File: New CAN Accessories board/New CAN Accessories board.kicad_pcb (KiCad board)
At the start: 2 copper layers, 110 x 86 mm, 108 parts, among them J1 39301040, J10 39301040, J11 ATF13-2P-BM03, J12 Conn_01x02_Pin, J13 Conn_01x12_Pin, J14 Conn_01x08_Pin, J2 39301040, J3 39301040, J4 39301040, J5 39301040, J6 39301040, J7 39301040, J8 39301040, J9 39301060, Q1 IRLML6344TRPBF, Q2 IRLML6344TRPBF, Q3 IRLML6344TRPBF, Q4 IRLML6344TRPBF, Q5 IRLML6344TRPBF, Q6 IRLML6344TRPBF, Q7 IRLML6344TRPBF, Q8 IRLML6344TRPBF, T1 MCP2562FD-E_SN, U1 NUCLEO_L432KC

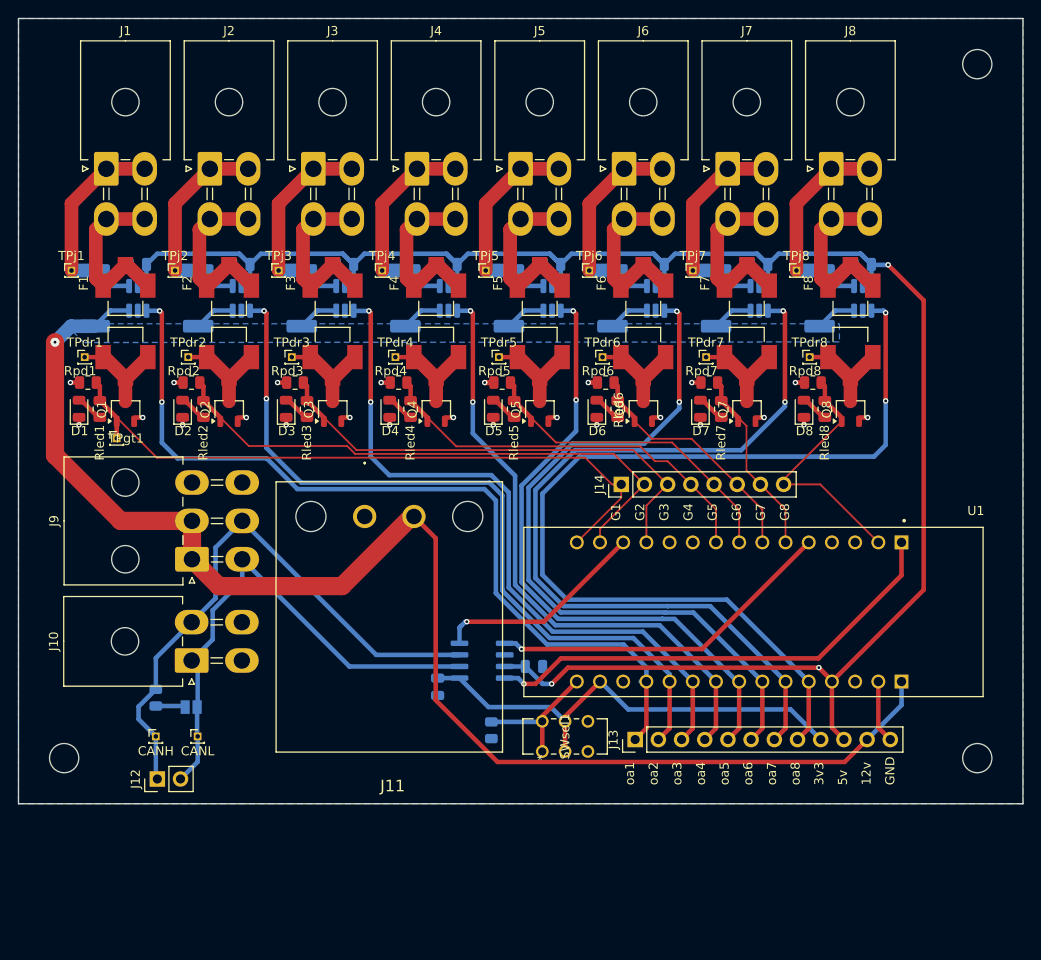
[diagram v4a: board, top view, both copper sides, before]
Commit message: added bulk cap
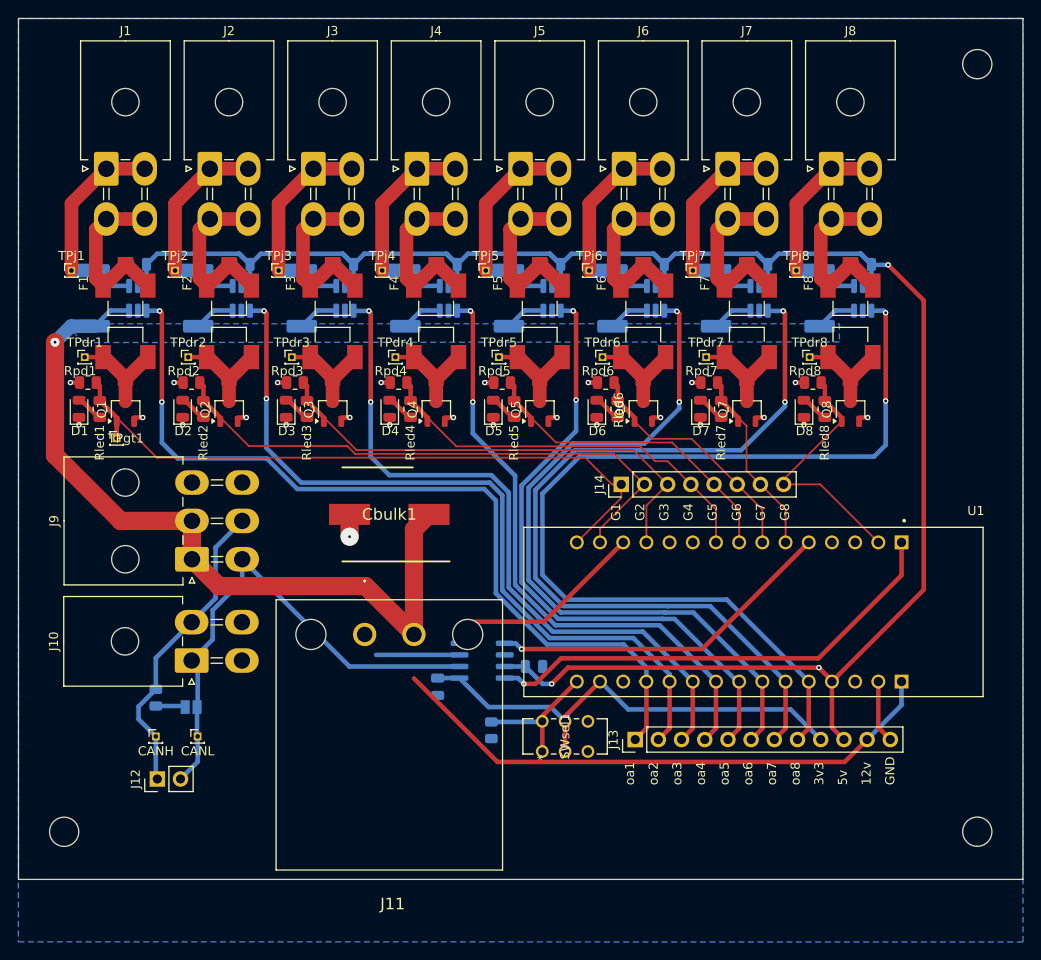
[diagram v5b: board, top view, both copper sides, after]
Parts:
- added Cbulk1: C_Polarized, footprint:CAPAE1030X1050M, F.Cu at (54.6, 68.3)
- moved J11 12.9 mm to (51.9, 81.5)
- moved H3 8.06 mm to (19.0, 103.1)
- moved H2 8.06 mm to (119.0, 103.1)
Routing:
- net /CANH: track 63.7 -> 42.9 mm
- net 12V: track 184.3 -> 179.6 mm
- net GND: track 52.9 -> 55.3 mm, vias 24 -> 25
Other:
- board size 110 x 86 mm -> 110 x 94.3 mm

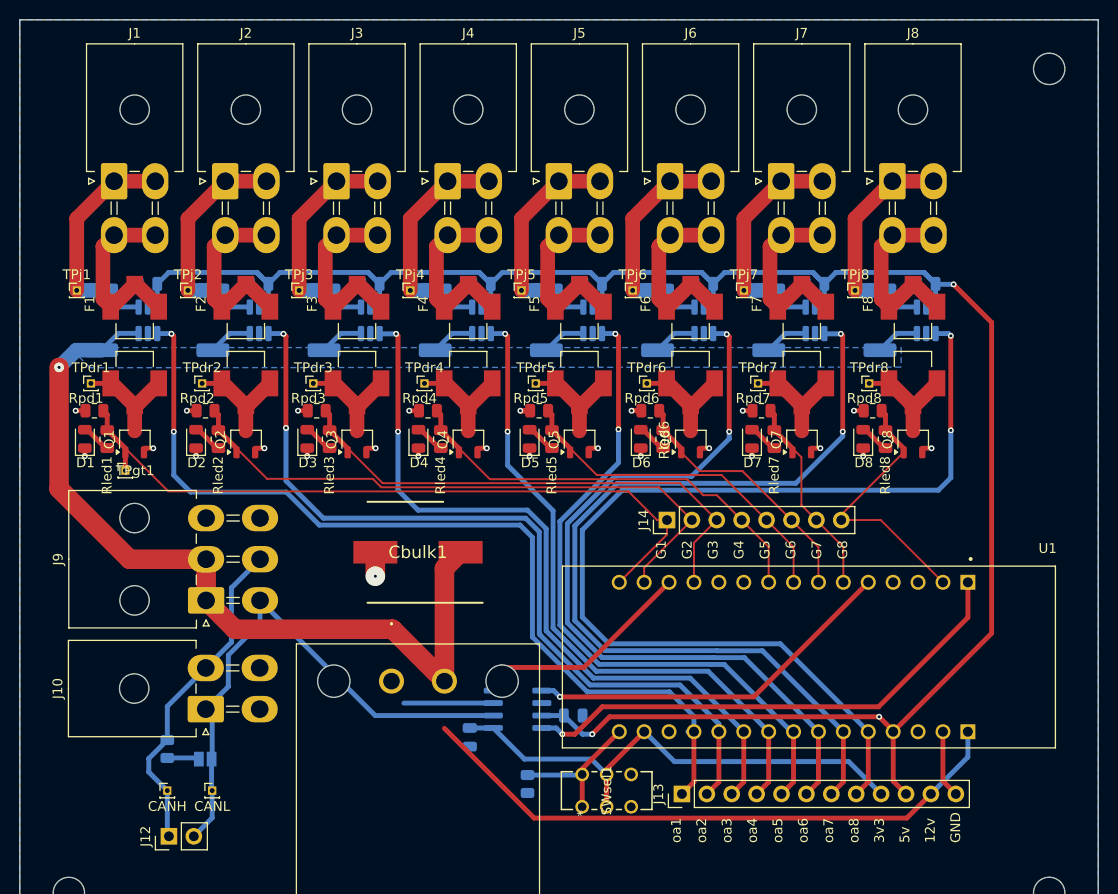
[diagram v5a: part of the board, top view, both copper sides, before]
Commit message: Added two 1x4 pin headers for J1-J8 - also fixed CAN module
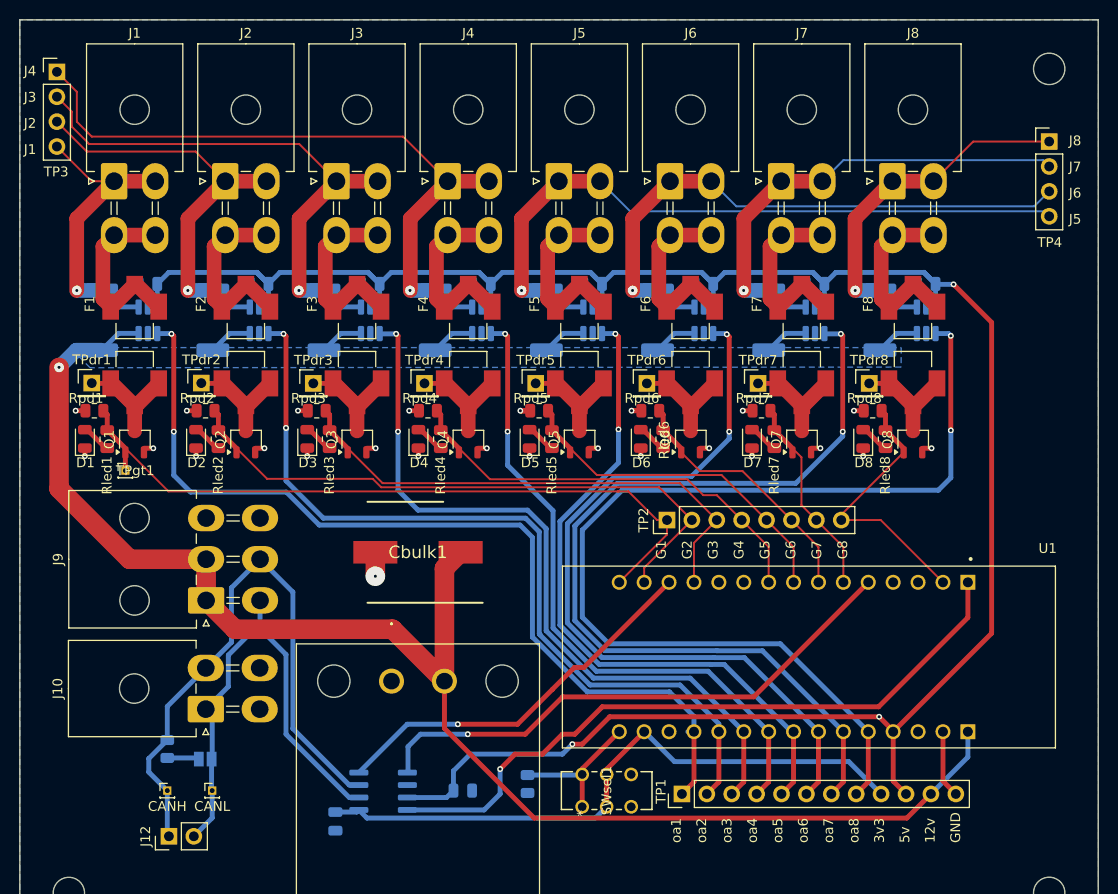
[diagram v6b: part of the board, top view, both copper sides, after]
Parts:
- removed TPj1, TPj2, TPj3, TPj4, TPj5, TPj6, TPj7, TPj8: TestPoint, Connector_PinHeader_1.00mm:PinHeader_1x01_P1.00mm_Vertical
- added TP3: Conn_01x04_Pin, Connector_PinHeader_2.54mm:PinHeader_1x04_P2.54mm_Vertical, F.Cu at (17.8, 19.3)
- added TP4: Conn_01x04_Pin, Connector_PinHeader_2.54mm:PinHeader_1x04_P2.54mm_Vertical, F.Cu at (119.0, 26.4)
- Cbulk1: value C_Polarized -> 270uF
- TPdr1, TPdr2, TPdr3, TPdr4, TPdr5, TPdr6, TPdr7, TPdr8: footprint Connector_PinHeader_1.00mm:PinHeader_1x01_P1.00mm_Vertical -> Connector_PinHeader_2.54mm:PinHeader_1x01_P2.54mm_Vertical
- moved Ctr2 16.2 mm to (46.2, 95.8)
- moved T1 16.1 mm to (51.1, 92.7)
- moved Ctr1 13.6 mm to (59.2, 92.6)
- moved TPdr1 0.09 mm to (21.3, 51.1)
- moved TPdr2 0.08 mm to (32.5, 51.1)
- renumbered J13 to TP1, J14 to TP2
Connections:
- net Net-(J1-Pin_1) renamed /TPj1
- net Net-(J2-Pin_1) renamed /TPj2
- net Net-(J3-Pin_1) renamed /TPj3
- net Net-(J4-Pin_1) renamed /TPj4
- net Net-(J5-Pin_1) renamed /TPj5
- net Net-(J6-Pin_1) renamed /TPj6
- net Net-(J7-Pin_1) renamed /TPj7
- net Net-(J8-Pin_1) renamed /TPj8
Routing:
- net /TPj5: track 23.9 -> 71.2 mm, vias 0 -> 1
- net /TPj4: track 23.9 -> 70.2 mm, vias 0 -> 1
- net /TPj6: track 23.9 -> 60.1 mm, vias 0 -> 1
- net /TPj3: track 23.9 -> 56.9 mm, vias 0 -> 1
- net /TPj7: track 23.9 -> 48.2 mm, vias 0 -> 1
- net /TPj2: track 23.9 -> 43.6 mm, vias 0 -> 1
- net /CANH: track 42.9 -> 61.6 mm
- net /CANTX: track 38.4 -> 56.6 mm
- net /CANRX: track 52.2 -> 70.4 mm
- net 5V: track 215.0 -> 231.8 mm
- net /STBY: track 23.5 -> 39.7 mm
- net /TPj8: track 23.9 -> 37.4 mm, vias 0 -> 1
- net /3V3: track 52.0 -> 64.6 mm
- net /TPj1: track 23.9 -> 31.2 mm, vias 0 -> 1
- net /CANL: track 56.1 -> 50.0 mm
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
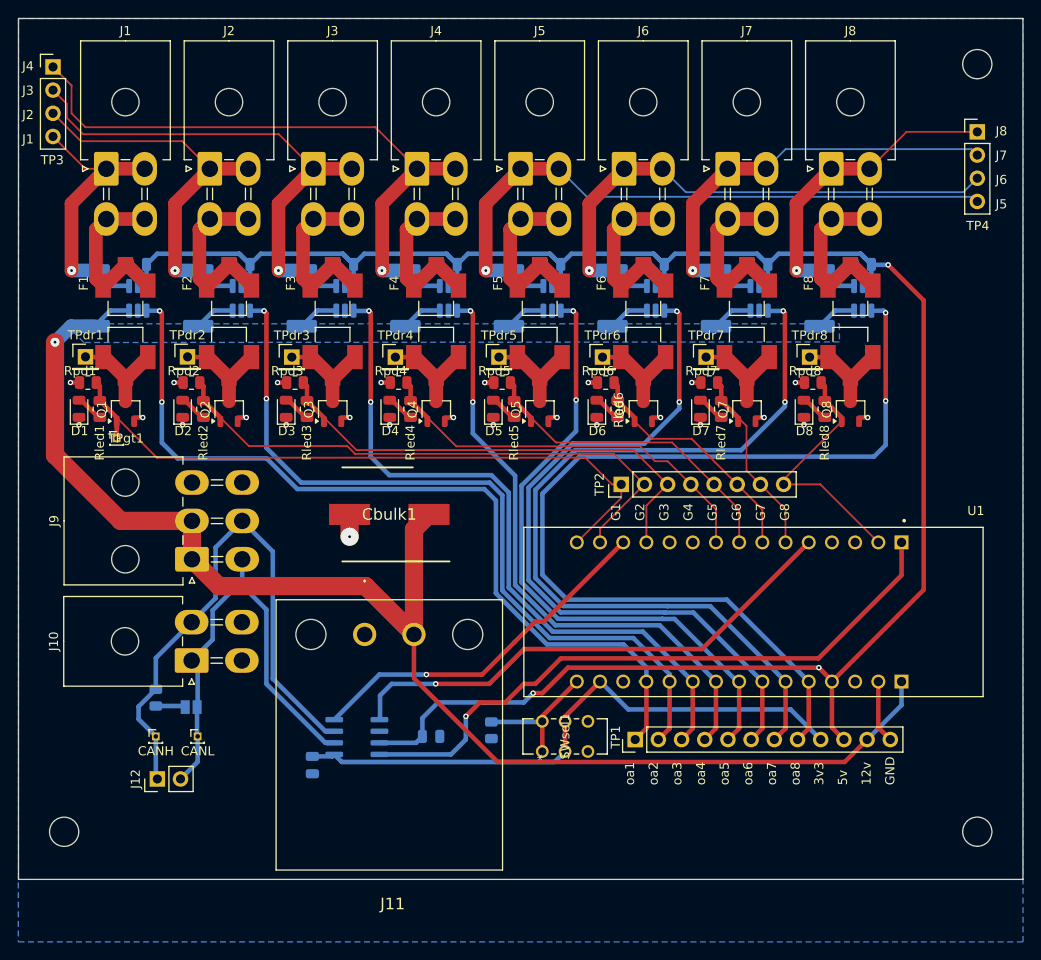
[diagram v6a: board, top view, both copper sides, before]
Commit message: few labelling changes
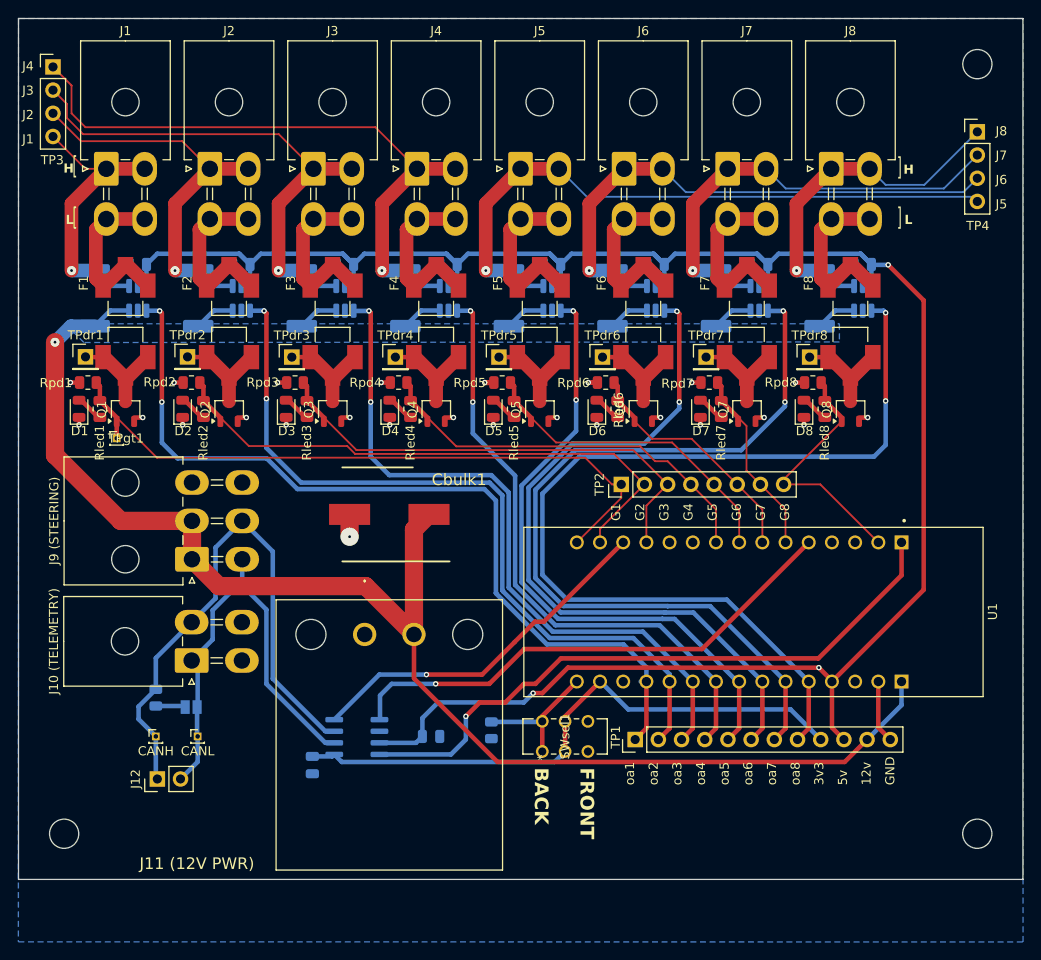
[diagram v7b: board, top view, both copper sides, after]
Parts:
- J10 (TELEMETRY): renamed from J10
- J11 (12V PWR): renamed from J11
- J9 (STEERING): renamed from J9
- moved H2 0.22 mm to (119.0, 103.3)
- moved H3 0.22 mm to (19.0, 103.3)
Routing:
- net /TPj8: track 37.4 -> 38.9 mm
- net /TPj7: track 48.2 -> 49.5 mm
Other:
- board text added: "BACK"
- board text added: "FRONT"
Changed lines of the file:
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@@
 		(tags "resistor")
 		(property "Reference" "Rpd1"
-			(at 0.852857 1.27 180)
+			(at 3.512857 -0.04 180)
 			(layer "F.SilkS")
 			(effects
@@
 		(tags "resistor")
 		(property "Reference" "Rpd4"
-			(at 0.852857 1.27 180)
+			(at 3.607143 0 180)
 			(layer "F.SilkS")
 			(effects
@@
 		(tags "resistor")
 		(property "Reference" "Rpd3"
-			(at 0.852857 1.27 180)
+			(at 3.545714 0.02 180)
 			(layer "F.SilkS")
 			(effects
@@
 			(layer "F.Fab")
 		)
+		(fp_text user "["
+			(at -3.7 0.83 0)
+			(unlocked yes)
+			(layer "F.SilkS")
+			(effects
+				(font
+					(size 2 1)
+					(thickness 0.1)
+				)
+				(justify left bottom)
+			)
+		)
+		(fp_text user "L"
+			(at -4.461905 6.164 0)
+			(unlocked yes)
+			(layer "F.SilkS")
+			(effects
+				(font
+					(size 1 1)
+					(thickness 0.2)
+					(bold yes)
+				)
+				(justify left bottom)
+			)
+		)
+		(fp_text user "["
+			(at -3.7 6.4545 0)
+			(unlocked yes)
+			(layer "F.SilkS")
+			(effects
+				(font
+					(size 2 1)
+					(thickness 0.1)
+				)
+				(justify left bottom)
+			)
+		)
+		(fp_text user "H"
+			(at -4.7 0.5395 0)
+			(unlocked yes)
+			(layer "F.SilkS")
+			(effects
+				(font
+					(size 1 1)
+					(thickness 0.2)
+					(bold yes)
+				)
+				(justify left bottom)
+			)
+		)
 		(fp_text user "${REFERENCE}"
 			(at 2.1 -13.2 0)
@@
 		(at 94.488 78.994 -90)
 		(property "Reference" "U1"
-			(at -11.08 -24.355 180)
+			(at -0.034 -26.202 90)
 			(layer "F.SilkS")
 			(effects
@@
 		(tags "resistor")
 		(property "Reference" "Rpd6"
-			(at 0.852857 1.27 180)
+			(at 3.53 -0.03 180)
 			(layer "F.SilkS")
 			(effects
@@
 	(footprint "MountingHole:MountingHole_3.2mm_M3_ISO14580"
 		(layer "F.Cu")
-		(at 19 103.065)
+		(at 19 103.28)
 		(descr "Mounting Hole 3.2mm, M3, no annular, generated by kicad-footprint-generator mountinghole.py")
 		(tags "mountinghole M3 ISO14580")
@@
 		(tags "resistor")
 		(property "Reference" "Rpd7"
-			(at 0.852857 1.27 180)
+			(at 3.481428 -0.1 180)
 			(layer "F.SilkS")
 			(effects
@@
 		(descr "Molex Mini-Fit Jr. Power Connectors, old mpn/engineering number: 5569-04A2, example for new mpn: 39-30-0040, 2 Pins per row, Mounting: Snap-in Plastic Peg PCB Lock (http://www.molex.com/pdm_docs/sd/039300020_sd.pdf), generated with kicad-footprint-generator")
 		(tags "connector Molex Mini-Fit_Jr horizontalplastic_peg")
-		(property "Reference" "J10"
+		(property "Reference" "J10 (TELEMETRY)"
 			(at 2.1 -15.1 90)
 			(layer "F.SilkS")
@@
 		(descr "ATF13-2P-BM03-1")
 		(tags "Connector")
-		(property "Reference" "J11"
-			(at 3.06 29.51 0)
+		(property "Reference" "J11 (12V PWR)"
+			(at -18.37 25.095 0)
 			(layer "F.SilkS")
 			(effects
@@
 		(descr "Molex Mini-Fit Jr. Power Connectors, old mpn/engineering number: 5569-06A2, example for new mpn: 39-30-0060, 3 Pins per row, Mounting: Snap-in Plastic Peg PCB Lock (http://www.molex.com/pdm_docs/sd/039300020_sd.pdf), generated with kicad-footprint-generator")
 		(tags "connector Molex Mini-Fit_Jr horizontalplastic_peg")
-		(property "Reference" "J9"
+		(property "Reference" "J9 (STEERING)"
 			(at 4.2 -15.1 90)
 			(layer "F.SilkS")
@@
 		(tags "resistor")
 		(property "Reference" "Rpd8"
-			(at 0.852857 1.27 180)
+			(at 3.502857 0.02 180)
 			(layer "F.SilkS")
 			(effects
@@
 		(tags "resistor")
 		(property "Reference" "Rpd5"
-			(at 0.852857 1.27 180)
+			(at 3.558571 -0.03 180)
 			(layer "F.SilkS")
 			(effects
@@
 			(layer "F.Fab")
 		)
+		(fp_text user "L"
+			(at 8.019047 6.164 0)
+			(unlocked yes)
+			(layer "F.SilkS")
+			(effects
+				(font
+					(size 1 1)
+					(thickness 0.2)
+					(bold yes)
+				)
+				(justify left bottom)
+			)
+		)
+		(fp_text user "H"
+			(at 7.9 0.664 0)
+			(unlocked yes)
+			(layer "F.SilkS")
+			(effects
+				(font
+					(size 1 1)
+					(thickness 0.2)
+					(bold yes)
+				)
+				(justify left bottom)
+			)
+		)
+		(fp_text user "]"
+			(at 7.2 6.4545 0)
+			(unlocked yes)
+			(layer "F.SilkS")
+			(effects
+				(font
+					(size 2 1)
+					(thickness 0.1)
+				)
+				(justify left bottom)
+			)
+		)
+		(fp_text user "]"
+			(at 7.2 0.9545 0)
+			(unlocked yes)
+			(layer "F.SilkS")
+			(effects
+				(font
+					(size 2 1)
+					(thickness 0.1)
+				)
+				(justify left bottom)
+			)
+		)
 		(fp_text user "${REFERENCE}"
 			(at 2.1 -13.2 0)
@@
 		(tags "Capacitor Polarised")
 		(property "Reference" "Cbulk1"
-			(at 0 0 180)
+			(at -7.65 3.8 180)
 			(layer "F.SilkS")
 			(effects
@@
 			(layer "F.Fab")
 		)
-		(fp_text user "${REFERENCE}"
-			(at 0 0 180)
-			(layer "F.Fab")
-			(effects
-				(font
-					(size 1.27 1.27)
-					(thickness 0.254)
-				)
-			)
-		)
 		(pad "1" smd rect
 			(at -4.35 0 270)
@@
 	(footprint "MountingHole:MountingHole_3.2mm_M3_ISO14580"
 		(layer "F.Cu")
-		(at 119 103.055)
+		(at 119 103.28)
 		(descr "Mounting Hole 3.2mm, M3, no annular, generated by kicad-footprint-generator mountinghole.py")
 		(tags "mountinghole M3 ISO14580")
@@
 	(footprint "MountingHole:MountingHole_3.2mm_M3_ISO14580"
 		(layer "F.Cu")
-		(at 119 19)
+		(at 119.01 19)
 		(descr "Mounting Hole 3.2mm, M3, no annular, generated by kicad-footprint-generator mountinghole.py")
 		(tags "mountinghole M3 ISO14580")
@@
 		(tags "resistor")
 		(property "Reference" "Rpd2"
-			(at 0.852857 1.27 180)
+			(at 3.484286 0.05 180)
 			(layer "F.SilkS")
 			(effects
@@
 		(layer "Edge.Cuts")
 	)
+	(gr_text "FRONT\n"
+		(at 75.364 96.03 270)
+		(layer "F.SilkS")
+		(effects
+			(font
+				(size 1.5 1.5)
+				(thickness 0.3)
+				(bold yes)
+			)
+			(justify left bottom)
+		)
+	)
+	(gr_text "BACK\n"
+		(at 70.364 96.03 270)
+		(layer "F.SilkS")
+		(effects
+			(font
+				(size 1.5 1.5)
+				(thickness 0.3)
+				(bold yes)
+			)
+			(justify left bottom)
+		)
+	)
 	(segment
 		(start 38.004286 57.7)
@@
 	)
 	(segment
-		(start 119 28.956)
-		(end 118.353 28.309)
-		(width 0.2)
-		(layer "B.Cu")
-		(net 65)
-	)
-	(segment
 		(start 92.071428 43.28)
 		(end 94.156477 43.28)
@@
 	)
 	(segment
-		(start 98.012428 28.309)
+		(start 115.337 32.619)
+		(end 98.020428 32.619)
+		(width 0.2)
+		(layer "B.Cu")
+		(net 65)
+	)
+	(segment
+		(start 98.020428 32.619)
 		(end 95.861428 30.46)
 		(width 0.2)
@@
 	)
 	(segment
-		(start 118.353 28.309)
-		(end 98.012428 28.309)
+		(start 119 28.956)
+		(end 115.337 32.619)
 		(width 0.2)
 		(layer "B.Cu")
@@
 	)
 	(segment
-		(start 119 26.416)
-		(end 111.246857 26.416)
-		(width 0.2)
-		(layer "F.Cu")
-		(net 66)
-	)
-	(segment
-		(start 111.246857 26.416)
-		(end 107.202857 30.46)
-		(width 0.2)
-		(layer "F.Cu")
-		(net 66)
-	)
-	(segment
 		(start 99.192857 41.61)
 		(end 99.192857 34.27)
@@
 	)
 	(segment
+		(start 108.960857 32.218)
+		(end 107.202857 30.46)
+		(width 0.2)
+		(layer "B.Cu")
+		(net 66)
+	)
+	(segment
+		(start 119 26.416)
+		(end 113.198 32.218)
+		(width 0.2)
+		(layer "B.Cu")
+		(net 66)
+	)
+	(segment
 		(start 99.202857 41.6)
 		(end 99.192857 41.61)
@@
 	)
 	(segment
+		(start 113.198 32.218)
+		(end 108.960857 32.218)
+		(width 0.2)
+		(layer "B.Cu")
+		(net 66)
+	)
+	(segment
 		(start 101.732857 41.6)
 		(end 99.202857 41.6)
@@
 		(polygon
 			(pts
-				(xy 113.65 108.055) (xy 124.01 108.055) (xy 124.01 98.165) (xy 113.661581 98.165)
+				(xy 113.649777 108.245) (xy 124.01 108.245) (xy 124.01 98.165) (xy 113.661581 98.165)
 			)
 		)
@@
 	)
 	(group ""
-		(members "7f9bcf5a-fc23-488e-aa72-52ec95ad7ee5" "8007bc1b-fe95-4f5d-8240-7e42b98ab722")
-	)
-	(group ""
-		(members "c71f6209-b89e-40a6-b6fd-e4613e896e21" "e77d81f8-8807-4246-adbf-48d6b3d2b4ce")
-	)
-	(group ""
